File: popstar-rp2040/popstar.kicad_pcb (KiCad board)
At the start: 2 copper layers, 284.7 x 94.2 mm, 182 parts, among them J1 JST SH 4-pin, J2 SWD, SW1 Boot, SW10 MX_SW_solder, SW11 MX_SW_solder, SW12 MX_SW_solder, SW13 MX_SW_solder, SW14 MX_SW_solder, SW15 MX_SW_solder, SW16 MX_SW_solder, SW17 MX_SW_solder, SW18 MX_SW_solder, SW19 MX_SW_solder, SW2 MX_SW_solder, SW20 MX_SW_solder, SW21 MX_SW_solder, SW22 MX_SW_solder, SW23 MX_SW_solder, SW24 MX_SW_solder, SW25 MX_SW_solder, SW26 MX_SW_solder, SW27 MX_SW_solder, SW28 MX_SW_solder, SW29 MX_SW_solder, SW3 MX_SW_solder, SW30 MX_SW_solder, SW31 MX_SW_solder, SW32 MX_SW_solder, SW33 MX_SW_solder, SW34 MX_SW_solder, SW35 MX_SW_solder, SW36 MX_SW_solder, SW37 MX_SW_solder, SW38 MX_SW_solder, SW39 MX_SW_solder, SW4 MX_SW_solder, SW40 MX_SW_solder, SW41 MX_SW_solder, SW42 MX_SW_solder, SW43 MX_SW_solder, SW44 MX_SW_solder, SW45 MX_SW_solder, SW46 MX_SW_solder, SW47 MX_SW_solder, SW48 MX_SW_solder, SW49 MX_SW_solder, SW5 MX_SW_solder, SW50 MX_SW_solder, SW51 MX_SW_solder, SW52 MX_SW_solder, SW53 MX_SW_solder, SW54 MX_SW_solder, SW55 MX_SW_solder, SW56 MX_SW_solder, SW57 MX_SW_solder, SW58 MX_SW_solder, SW59 MX_SW_solder, SW6 MX_SW_solder, SW60 MX_SW_solder, SW61 MX_SW_solder, SW62 MX_SW_solder, SW7 MX_SW_solder, SW8 MX_SW_solder, SW9 MX_SW_solder, U2 XC6206PxxxMR, U3 SRV05-4, U4 W25Q128JVS, U5 74AHCT1G125, U6 RP2040, Y1 12MHz

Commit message: Fixed more DRC errors, routed columns, added front Cu on GND pins for MCU
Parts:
- moved D52 1.01 mm to (303.0, 74.6)
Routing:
- net COL13: track 8.43 -> 284.9 mm
- net COL12: track 10.0 -> 246.6 mm
- net COL11: track 9.47 -> 214.3 mm
- net COL10: track 8.47 -> 194.1 mm
- net COL09: track 7.57 -> 173.7 mm
- net COL08: track 6.94 -> 154.1 mm
- net COL07: track 7.61 -> 134.6 mm
- net COL06: track 12.3 -> 115.0 mm
- net GND: track 74.5 -> 112.8 mm
- net +1V1: track 14.8 -> 30.2 mm, vias 1 -> 4
- net +3V3: track 48.5 -> 45.8 mm
- net ROW2: track 306.6 -> 304.3 mm
- net Net-(D52-A): track 5.95 -> 4.94 mm
- net COL02: track 82.5 -> 81.8 mm
- net ROW1: track 314.6 -> 315.2 mm

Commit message: Finished routing columns for rows 2, 3, 4
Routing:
- net COL13: track 284.9 -> 374.1 mm
- net COL12: track 246.6 -> 303.2 mm
- net COL11: track 214.3 -> 267.3 mm
- net COL10: track 194.1 -> 242.3 mm
- net COL08: track 154.1 -> 198.6 mm
- net COL09: track 173.7 -> 217.7 mm
- net COL07: track 134.6 -> 178.6 mm
- net COL06: track 115.0 -> 159.0 mm
- net COL05: track 94.0 -> 138.0 mm
- net COL04: track 73.9 -> 117.9 mm
- net COL03: track 54.4 -> 98.4 mm
- net ROW2: track 304.3 -> 302.9 mm

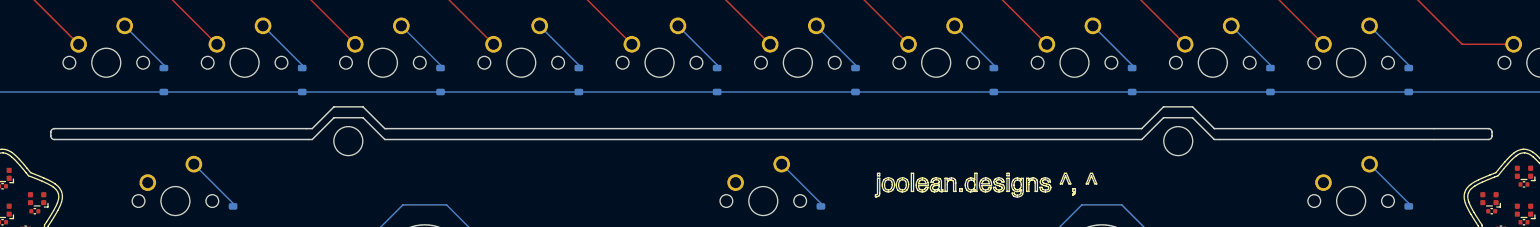
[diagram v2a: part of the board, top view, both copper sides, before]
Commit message: Finshed routing columns for row 5
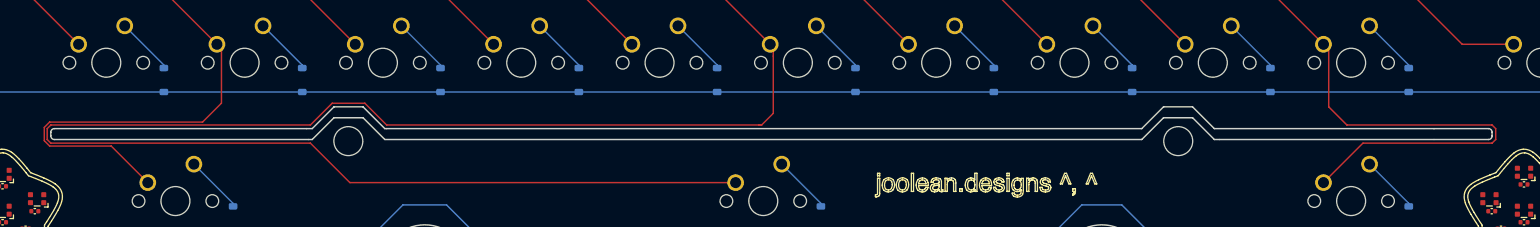
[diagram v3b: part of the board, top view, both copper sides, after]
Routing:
- net COL06: track 159.0 -> 371.3 mm
- net COL10: track 242.3 -> 303.1 mm
- net COL02: track 81.8 -> 134.4 mm
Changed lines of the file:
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@@
   (segment (start 39.25 63.75) (end 39.25 49.25) (width 0.2) (layer "B.Cu") (net 97))
   (segment (start 89.8525 66.83375) (end 85.725 62.70625) (width 0.2) (layer "F.Cu") (net 98))
+  (segment (start 84.8175 109.9) (end 89.8525 114.935) (width 0.2) (layer "F.Cu") (net 98))
   (segment (start 89.8525 76.835) (end 90.4875 77.47) (width 0.2) (layer "F.Cu") (net 98))
+  (segment (start 100 96.5) (end 100 104) (width 0.2) (layer "F.Cu") (net 98))
   (segment (start 90.4875 86.995) (end 99.3775 95.885) (width 0.2) (layer "F.Cu") (net 98))
+  (segment (start 100 104) (end 97.4 106.6) (width 0.2) (layer "F.Cu") (net 98))
+  (segment (start 99.3775 95.885) (end 99.385 95.885) (width 0.2) (layer "F.Cu") (net 98))
+  (segment (start 76.334315 109.9) (end 84.8175 109.9) (width 0.2) (layer "F.Cu") (net 98))
+  (segment (start 75.6 109.165686) (end 76.334315 109.9) (width 0.2) (layer "F.Cu") (net 98))
+  (segment (start 99.385 95.885) (end 100 96.5) (width 0.2) (layer "F.Cu") (net 98))
+  (segment (start 75.6 107.334315) (end 75.6 109.165686) (width 0.2) (layer "F.Cu") (net 98))
   (segment (start 90.4875 77.47) (end 90.4875 86.995) (width 0.2) (layer "F.Cu") (net 98))
   (segment (start 85.725 62.70625) (end 85.725 58.42) (width 0.2) (layer "F.Cu") (net 98))
   (segment (start 85.725 58.42) (end 85.09 57.785) (width 0.2) (layer "F.Cu") (net 98))
+  (segment (start 97.4 106.6) (end 76.334314 106.6) (width 0.2) (layer "F.Cu") (net 98))
+  (segment (start 76.334314 106.6) (end 75.6 107.334315) (width 0.2) (layer "F.Cu") (net 98))
   (segment (start 89.8525 76.835) (end 89.8525 66.83375) (width 0.2) (layer "F.Cu") (net 98))
   (segment (start 62.386194 73.443915) (end 64.7 75.757724) (width 0.2) (layer "B.Cu") (net 98))
@@
   (segment (start 63.5 76.254778) (end 63.500001 77.224876) (width 0.2) (layer "B.Cu") (net 101))
   (segment (start 63.122611 75.877389) (end 63.5 76.254778) (width 0.2) (layer "B.Cu") (net 101))
+  (segment (start 176 97.5) (end 176 105.4) (width 0.2) (layer "F.Cu") (net 102))
+  (segment (start 117.685 114.935) (end 170.815 114.935) (width 0.2) (layer "F.Cu") (net 102))
+  (segment (start 112.25 107) (end 76.5 107) (width 0.2) (layer "F.Cu") (net 102))
   (segment (start 166.5 77.2825) (end 166.5 86.8075) (width 0.2) (layer "F.Cu") (net 102))
   (segment (start 166.5 86.8075) (end 175.5775 95.885) (width 0.2) (layer "F.Cu") (net 102))
+  (segment (start 76 109) (end 76.5 109.5) (width 0.2) (layer "F.Cu") (net 102))
   (segment (start 162 58.495) (end 161.29 57.785) (width 0.2) (layer "F.Cu") (net 102))
   (segment (start 166.0525 76.835) (end 166.5 77.2825) (width 0.2) (layer "F.Cu") (net 102))
+  (segment (start 76.5 109.5) (end 112.25 109.5) (width 0.2) (layer "F.Cu") (net 102))
+  (segment (start 76.5 107) (end 76 107.5) (width 0.2) (layer "F.Cu") (net 102))
   (segment (start 166.0525 76.835) (end 162 72.7825) (width 0.2) (layer "F.Cu") (net 102))
+  (segment (start 122.75 107) (end 119.75 104) (width 0.2) (layer "F.Cu") (net 102))
+  (segment (start 76 107.5) (end 76 109) (width 0.2) (layer "F.Cu") (net 102))
+  (segment (start 174.4 107) (end 122.75 107) (width 0.2) (layer "F.Cu") (net 102))
   (segment (start 162 72.7825) (end 162 58.495) (width 0.2) (layer "F.Cu") (net 102))
+  (segment (start 115.25 104) (end 112.25 107) (width 0.2) (layer "F.Cu") (net 102))
+  (segment (start 174.4 107) (end 174 107) (width 0.2) (layer "F.Cu") (net 102))
+  (segment (start 175.5775 95.885) (end 176 96.3075) (width 0.2) (layer "F.Cu") (net 102))
+  (segment (start 176 105.4) (end 174.4 107) (width 0.2) (layer "F.Cu") (net 102))
+  (segment (start 112.25 109.5) (end 117.685 114.935) (width 0.2) (layer "F.Cu") (net 102))
+  (segment (start 119.75 104) (end 115.25 104) (width 0.2) (layer "F.Cu") (net 102))
+  (segment (start 176 96.3075) (end 176 97.5) (width 0.2) (layer "F.Cu") (net 102))
   (segment (start 60.97198 74.858129) (end 62 75.886149) (width 0.2) (layer "B.Cu") (net 102))
   (segment (start 154.05625 84.94375) (end 162.165 76.835) (width 0.2) (layer "B.Cu") (net 102))
@@
   (segment (start 243 77.5825) (end 243 87.1075) (width 0.2) (layer "F.Cu") (net 106))
   (segment (start 242.2525 76.835) (end 243 77.5825) (width 0.2) (layer "F.Cu") (net 106))
+  (segment (start 252.5 96.6075) (end 252.5 104.5) (width 0.2) (layer "F.Cu") (net 106))
   (segment (start 242.2525 78.912588) (end 238 74.660088) (width 0.2) (layer "F.Cu") (net 106))
   (segment (start 242.2525 76.835) (end 242.2525 78.912588) (width 0.2) (layer "F.Cu") (net 106))
+  (segment (start 255 107) (end 275 107) (width 0.2) (layer "F.Cu") (net 106))
+  (segment (start 275.5 109) (end 275 109.5) (width 0.2) (layer "F.Cu") (net 106))
+  (segment (start 257.2125 109.5) (end 251.7775 114.935) (width 0.2) (layer "F.Cu") (net 106))
   (segment (start 243 87.1075) (end 251.7775 95.885) (width 0.2) (layer "F.Cu") (net 106))
+  (segment (start 275 107) (end 275.5 107.5) (width 0.2) (layer "F.Cu") (net 106))
   (segment (start 238 74.660088) (end 238 58.295) (width 0.2) (layer "F.Cu") (net 106))
+  (segment (start 252.5 104.5) (end 255 107) (width 0.2) (layer "F.Cu") (net 106))
   (segment (start 238 58.295) (end 237.49 57.785) (width 0.2) (layer "F.Cu") (net 106))
+  (segment (start 251.7775 95.885) (end 252.5 96.6075) (width 0.2) (layer "F.Cu") (net 106))
+  (segment (start 275.5 107.5) (end 275.5 109) (width 0.2) (layer "F.Cu") (net 106))
+  (segment (start 275 109.5) (end 257.2125 109.5) (width 0.2) (layer "F.Cu") (net 106))
   (segment (start 58.679689 75.966016) (end 58.679689 77) (width 0.2) (layer "B.Cu") (net 106))
   (segment (start 65.546695 82.1) (end 69.990451 86.54375) (width 0.2) (layer "B.Cu") (net 106))

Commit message: Finished routing columns for row 1
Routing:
- net COL07: track 178.6 -> 399.1 mm
- net COL06: track 371.3 -> 572.8 mm
- net COL08: track 198.6 -> 381.6 mm
- net COL05: track 138.0 -> 302.7 mm
- net COL09: track 217.7 -> 363.7 mm
- net COL04: track 117.9 -> 245.3 mm
- net COL10: track 303.1 -> 411.9 mm
- net COL03: track 98.4 -> 188.7 mm
- net COL11: track 267.3 -> 339.0 mm
- net COL02: track 134.4 -> 187.6 mm
- net COL12: track 303.2 -> 337.3 mm

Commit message: Changed column trace to front for right ctrl
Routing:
- net COL13: track 374.1 -> 394.1 mm
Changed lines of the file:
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@@
   (segment (start 57.879689 77.331372) (end 59.6 79.051683) (width 0.2) (layer "B.Cu") (net 108))
   (segment (start 294.64 38.735) (end 285.115 38.735) (width 0.2) (layer "F.Cu") (net 109))
+  (segment (start 311 97) (end 313 95) (width 0.2) (layer "F.Cu") (net 109))
+  (segment (start 313 85) (end 305 77) (width 0.2) (layer "F.Cu") (net 109))
+  (segment (start 300 66) (end 300 58.3825) (width 0.2) (layer "F.Cu") (net 109))
+  (segment (start 311 103.3375) (end 311 97) (width 0.2) (layer "F.Cu") (net 109))
   (segment (start 305 39.57) (end 304.165 38.735) (width 0.2) (layer "F.Cu") (net 109))
+  (segment (start 305 71) (end 300 66) (width 0.2) (layer "F.Cu") (net 109))
+  (segment (start 305 77) (end 305 71) (width 0.2) (layer "F.Cu") (net 109))
   (segment (start 304.165 38.735) (end 294.64 38.735) (width 0.2) (layer "F.Cu") (net 109))
   (segment (start 305 52.1875) (end 305 39.57) (width 0.2) (layer "F.Cu") (net 109))
+  (segment (start 313 95) (end 313 85) (width 0.2) (layer "F.Cu") (net 109))
+  (segment (start 299.4025 114.935) (end 311 103.3375) (width 0.2) (layer "F.Cu") (net 109))
+  (segment (start 300 58.3825) (end 299.4025 57.785) (width 0.2) (layer "F.Cu") (net 109))
   (segment (start 299.4025 57.785) (end 305 52.1875) (width 0.2) (layer "F.Cu") (net 109))
-  (segment (start 299.4025 112.0975) (end 299.4025 114.935) (width 0.2) (layer "B.Cu") (net 109))
   (segment (start 300 58.3825) (end 299.4025 57.785) (width 0.2) (layer "B.Cu") (net 109))
   (segment (start 304.9 70.834314) (end 300 65.934314) (width 0.2) (layer "B.Cu") (net 109))
@@
   (segment (start 64.5 83.3) (end 65.049639 83.3) (width 0.2) (layer "B.Cu") (net 109))
   (segment (start 57.479689 77.497057) (end 59.2 79.217368) (width 0.2) (layer "B.Cu") (net 109))
-  (segment (start 301 83.5) (end 310.5 83.5) (width 0.2) (layer "B.Cu") (net 109))
-  (segment (start 311 100.5) (end 299.4025 112.0975) (width 0.2) (layer "B.Cu") (net 109))
-  (segment (start 314 94) (end 311 97) (width 0.2) (layer "B.Cu") (net 109))
   (segment (start 69.493396 87.74375) (end 269.984436 87.74375) (width 0.2) (layer "B.Cu") (net 109))
   (segment (start 57.479689 75.468961) (end 57.479689 77.497057) (width 0.2) (layer "B.Cu") (net 109))
@@
   (segment (start 59.2 79.217368) (end 59.200002 81.159802) (width 0.2) (layer "B.Cu") (net 109))
   (segment (start 303 83.5) (end 304.9 81.6) (width 0.2) (layer "B.Cu") (net 109))
-  (segment (start 314 87) (end 314 94) (width 0.2) (layer "B.Cu") (net 109))
   (segment (start 58.09052 74.858129) (end 57.479689 75.468961) (width 0.2) (layer "B.Cu") (net 109))
   (segment (start 59.200002 81.159802) (end 61.3402 83.3) (width 0.2) (layer "B.Cu") (net 109))
-  (segment (start 310.5 83.5) (end 314 87) (width 0.2) (layer "B.Cu") (net 109))
   (segment (start 64.5 83.3) (end 65.04964 83.3) (width 0.2) (layer "B.Cu") (net 109))
-  (segment (start 311 97) (end 311 100.5) (width 0.2) (layer "B.Cu") (net 109))
   (segment (start 269.984436 87.74375) (end 274.228186 83.5) (width 0.2) (layer "B.Cu") (net 109))
   (segment (start 301 83.5) (end 303 83.5) (width 0.2) (layer "B.Cu") (net 109))
